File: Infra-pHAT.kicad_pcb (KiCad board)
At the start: 2 copper layers, 65 x 30 mm, 25 parts, among them Q1 BC817, U1 CAT24C32WI-GT3

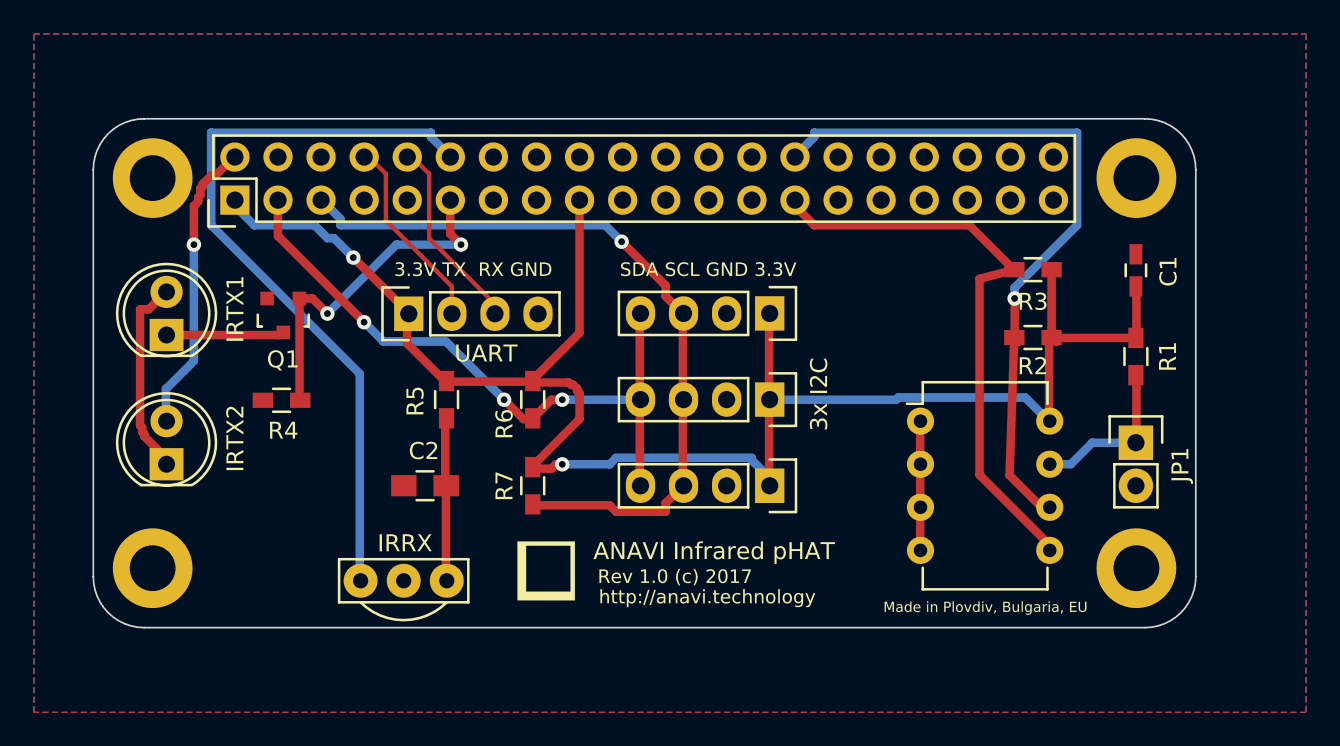
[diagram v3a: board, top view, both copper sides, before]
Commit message: Infra-pHAT.*: Add a current limiting resistor
Add a current limiting resistor for the IR LEDs.

Suggested-by: Norman Rasmussen <norman@rasmussen.co.za>
Signed-off-by: Leon Anavi <leon@anavi.org>
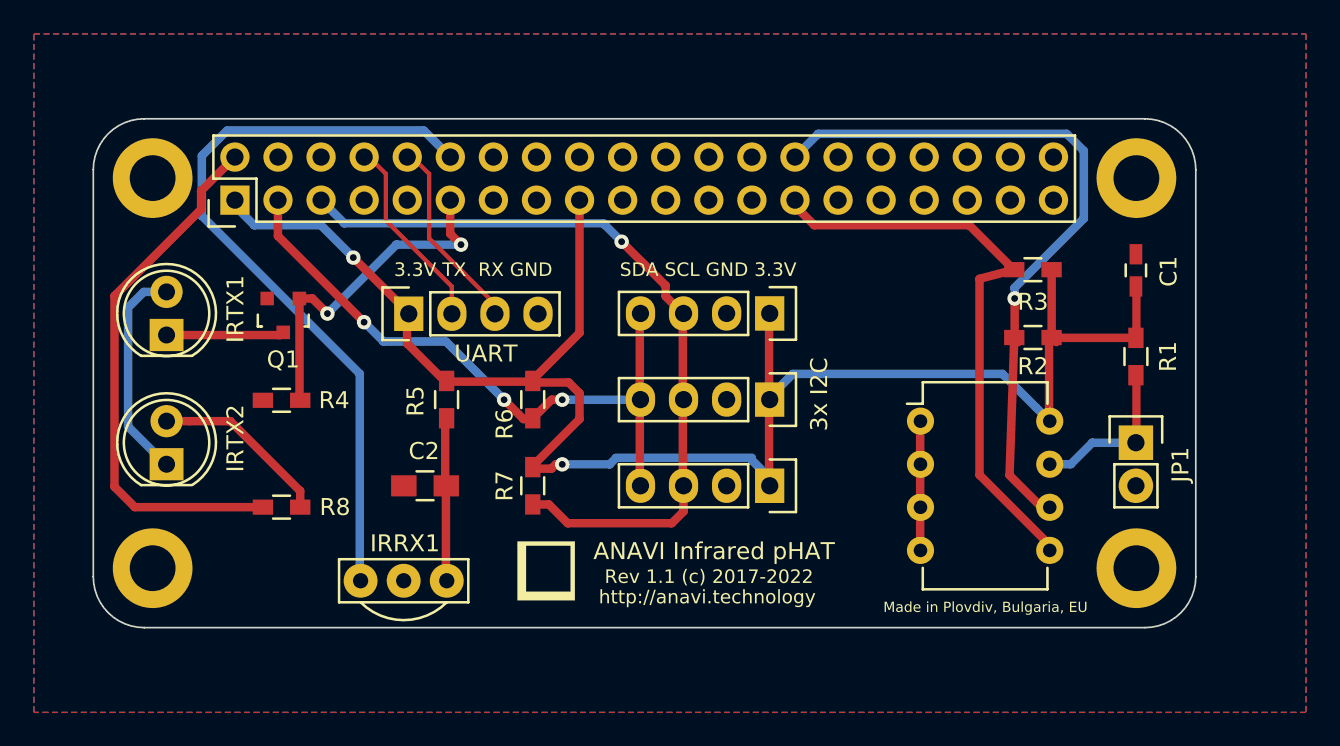
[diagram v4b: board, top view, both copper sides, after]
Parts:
- added R8: 36R, Resistors_SMD:R_0603_HandSoldering, F.Cu at (159.6, 97.9)
- renumbered IRRX to IRRX1
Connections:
- IRTX2 pad 2: +5V -> Net-(IRTX2-Pad2)
- RASP_CONN1 pad 13: Net-(RASP_CONN1-Pad13) -> (no net)
- RASP_CONN1 pad 15: Net-(RASP_CONN1-Pad15) -> (no net)
- RASP_CONN1 pad 16: Net-(RASP_CONN1-Pad16) -> (no net)
- RASP_CONN1 pad 18: Net-(RASP_CONN1-Pad18) -> (no net)
- RASP_CONN1 pad 19: Net-(RASP_CONN1-Pad19) -> (no net)
- RASP_CONN1 pad 21: Net-(RASP_CONN1-Pad21) -> (no net)
- RASP_CONN1 pad 22: Net-(RASP_CONN1-Pad22) -> (no net)
- RASP_CONN1 pad 23: Net-(RASP_CONN1-Pad23) -> (no net)
- RASP_CONN1 pad 24: Net-(RASP_CONN1-Pad24) -> (no net)
- RASP_CONN1 pad 26: Net-(RASP_CONN1-Pad26) -> (no net)
- RASP_CONN1 pad 29: Net-(RASP_CONN1-Pad29) -> (no net)
- RASP_CONN1 pad 31: Net-(RASP_CONN1-Pad31) -> (no net)
- RASP_CONN1 pad 32: Net-(RASP_CONN1-Pad32) -> (no net)
- RASP_CONN1 pad 33: Net-(RASP_CONN1-Pad33) -> (no net)
- RASP_CONN1 pad 35: Net-(RASP_CONN1-Pad35) -> (no net)
- RASP_CONN1 pad 36: Net-(RASP_CONN1-Pad36) -> (no net)
- RASP_CONN1 pad 37: Net-(RASP_CONN1-Pad37) -> (no net)
- RASP_CONN1 pad 38: Net-(RASP_CONN1-Pad38) -> (no net)
- RASP_CONN1 pad 40: Net-(RASP_CONN1-Pad40) -> (no net)
- RASP_CONN1 pad 7: Net-(RASP_CONN1-Pad7) -> (no net)
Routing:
- net +5V: track 17.5 -> 31.7 mm, vias 1 -> 0
- net Net-(IRTX2-Pad2): track 0.00 -> 10.6 mm
- net Net-(IRTX1-Pad2): track 11.8 -> 13.3 mm
- net +3V3: track 105.5 -> 106.7 mm
- net Net-(R7-Pad2): track 45.2 -> 46.1 mm
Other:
- board text added: "Rev 1.1 (c) 2017-2022"
- board text removed: "Rev 1.0 (c) 2017"
